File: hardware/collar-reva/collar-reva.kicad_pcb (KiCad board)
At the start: 2 copper layers, 30 x 30 mm, 0 parts

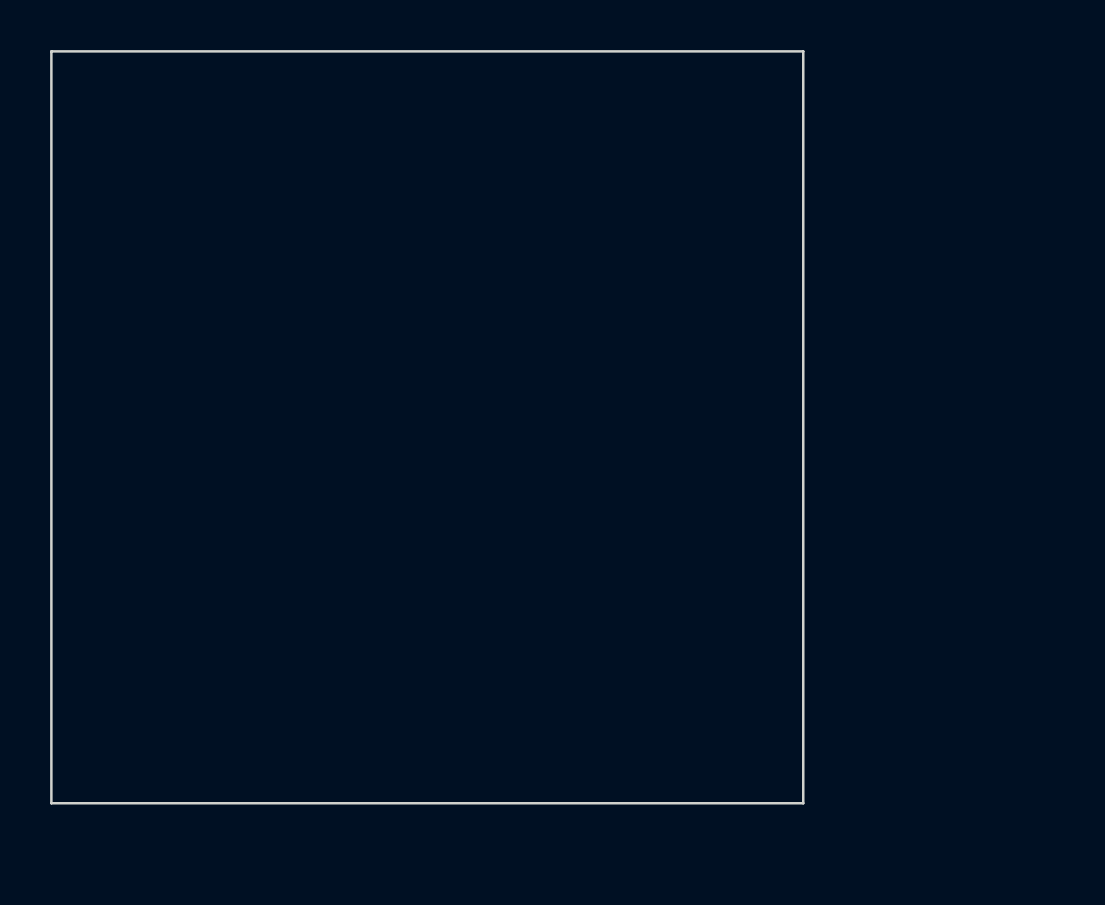
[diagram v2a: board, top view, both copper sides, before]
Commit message: feat(hw): place Rev-A parts on a 40×32 mm board
30×30 cannot fit the module and USB-C. Dirty/charge, brain, and optical zones are now footprints on the outline; copper is still unrouted.

Co-authored-by: Cursor <cursoragent@cursor.com>
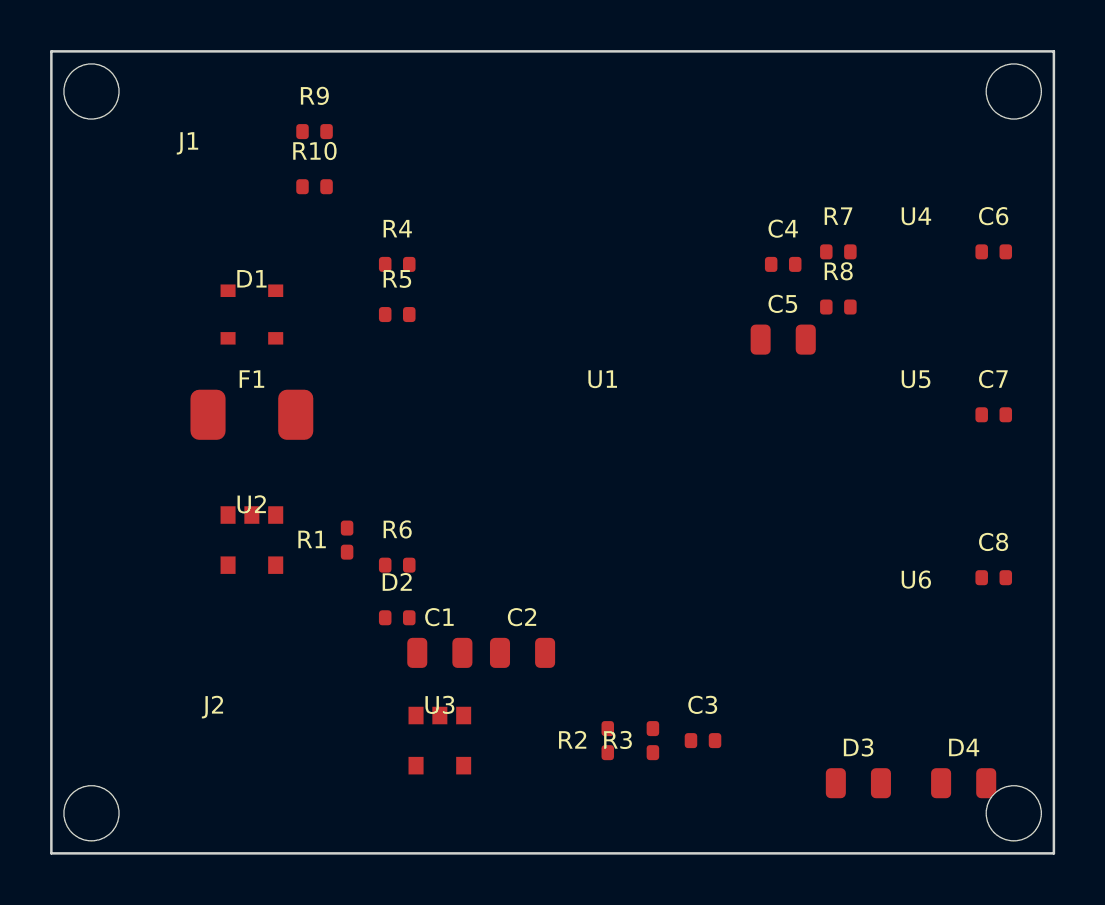
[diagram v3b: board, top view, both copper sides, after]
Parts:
- added C1: 10uF 16V, Capacitor_SMD:C_0805_2012Metric, F.Cu at (115.5, 104.0)
- added C2: 10uF 16V, Capacitor_SMD:C_0805_2012Metric, F.Cu at (118.8, 104.0)
- added C3: 100nF 16V, Capacitor_SMD:C_0402_1005Metric, F.Cu at (126.0, 107.5)
- added C4: 100nF 16V, Capacitor_SMD:C_0402_1005Metric, F.Cu at (129.2, 88.5)
- added C5: 10uF 16V, Capacitor_SMD:C_0805_2012Metric, F.Cu at (129.2, 91.5)
- added C6: 100nF 16V, Capacitor_SMD:C_0402_1005Metric, F.Cu at (137.6, 88.0)
- added C7: 100nF 16V, Capacitor_SMD:C_0402_1005Metric, F.Cu at (137.6, 94.5)
- added C8: 100nF 16V, Capacitor_SMD:C_0402_1005Metric, F.Cu at (137.6, 101.0)
- added D1: USBLC6-2SC6, Package_TO_SOT_SMD:SOT-23-6, F.Cu at (108.0, 90.5)
- added D2: Green LED, LED_SMD:LED_0402_1005Metric, F.Cu at (113.8, 102.6)
- added D3: 940 nm IR LED, LED_SMD:LED_0805_2012Metric, F.Cu at (132.2, 109.2)
- added D4: 940 nm photodiode, Diode_SMD:D_0805_2012Metric, F.Cu at (136.4, 109.2)
- added F1: PTC 500 mA, Fuse:Fuse_1812_4532Metric, F.Cu at (108.0, 94.5)
- added H: , MountingHole:MountingHole_2.2mm, F.Cu at (101.6, 81.6)
- added H: , MountingHole:MountingHole_2.2mm, F.Cu at (138.4, 81.6)
- added H: , MountingHole:MountingHole_2.2mm, F.Cu at (101.6, 110.4)
- added H: , MountingHole:MountingHole_2.2mm, F.Cu at (138.4, 110.4)
- added J1: USB-C receptacle, Connector_USB:USB_C_Receptacle_USB4105-xx-A_16P_TopMnt_Horizontal, F.Cu at (105.5, 85.0)
- added J2: JST-PH 2, Connector_JST:JST_PH_S2B-PH-SM4-TB_1x02-1MP_P2.00mm_Horizontal, F.Cu at (106.5, 107.5)
- added R1: 10k, Resistor_SMD:R_0402_1005Metric, F.Cu at (111.8, 99.5)
- added R10: 5.1k, Resistor_SMD:R_0402_1005Metric, F.Cu at (110.5, 85.4)
- added R2: 100k, Resistor_SMD:R_0402_1005Metric, F.Cu at (122.2, 107.5)
- added R3: 100k, Resistor_SMD:R_0402_1005Metric, F.Cu at (124.0, 107.5)
- added R4: 10k, Resistor_SMD:R_0402_1005Metric, F.Cu at (113.8, 88.5)
- added R5: 10k, Resistor_SMD:R_0402_1005Metric, F.Cu at (113.8, 90.5)
- added R6: 330, Resistor_SMD:R_0402_1005Metric, F.Cu at (113.8, 100.5)
- added R7: 4.7k, Resistor_SMD:R_0402_1005Metric, F.Cu at (131.4, 88.0)
- added R8: 4.7k, Resistor_SMD:R_0402_1005Metric, F.Cu at (131.4, 90.2)
- added R9: 5.1k, Resistor_SMD:R_0402_1005Metric, F.Cu at (110.5, 83.2)
- added U1: ESP32-S3-MINI-1-N8, RF_Module:ESP32-S3-MINI-1, F.Cu at (122.0, 94.5)
- added U2: MCP73831 4.2 V, Package_TO_SOT_SMD:SOT-23-5, F.Cu at (108.0, 99.5)
- added U3: AP2112K-3.3 600 mA, Package_TO_SOT_SMD:SOT-23-5, F.Cu at (115.5, 107.5)
- added U4: BMI270, Sensor_Motion:Bosch_LGA-14_2.5x3mm_P0.5mm_ClockwisePinNumbering, F.Cu at (134.5, 88.0)
- added U5: INMP441, Sensor_Audio:InvenSense_INMP441, F.Cu at (134.5, 94.5)
- added U6: AFE4404, Package_BGA:Texas_DSBGA-15_1.91x1.91mm_Layout5x3_P0.4mm, F.Cu at (134.5, 102.5)
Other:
- board size 30 x 30 mm -> 40 x 32 mm
- board text added: "RF_KEEP"

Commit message: feat(collar): emit gyro, die temp, and neck NTC on the 1 Hz map
The BMI270 and AFE already had unused channels. Turn them on and stuff the missing red LED plus contact NTC so the same notify map can carry chemistry-adjacent proxies without a new protocol.

Co-authored-by: Cursor <cursoragent@cursor.com>
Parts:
- added D5: 660 nm red LED, LED_SMD:LED_0805_2012Metric, F.Cu at (134.3, 106.8)
- added R11: 10k, Resistor_SMD:R_0402_1005Metric, F.Cu at (127.8, 106.8)
- added RT1: 10k NTC β3950, Resistor_SMD:R_0402_1005Metric, F.Cu at (127.8, 109.2)
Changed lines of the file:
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@@
+    )
+  )
+  (footprint "LED_SMD:LED_0805_2012Metric" (layer "F.Cu")
+    (at 134.3 106.8 0)
+    (attr smd)
+    (property "Reference" "D5" (at 0 -1.4 0)
+      (layer "F.SilkS")
+      (effects (font (size 0.7 0.7)))
+    )
+    (property "Value" "660 nm red LED" (at 0 1.4 0)
+      (layer "F.Fab")
+      (effects (font (size 0.6 0.6)))
+    )
+    (property "Footprint" "LED_SMD:LED_0805_2012Metric" (at 0 0 0)
+      (layer "F.Fab")
+      (effects (font (size 1.27 1.27)) hide)
+    )
+    (fp_rect (start -1.1 -0.8) (end 1.1 0.8)
+      (stroke (width 0.05) (type default)) (fill none) (layer "F.CrtYd")
+    )
+    (fp_rect (start -1.1 -0.8) (end 1.1 0.8)
+      (stroke (width 0.12) (type default)) (fill none) (layer "F.Fab")
+    )
+    (pad "1" smd roundrect (at -0.9 0) (size 0.8 1.2) (layers "F.Cu" "F.Paste" "F.Mask")
+      (roundrect_rratio 0.25)
+    )
+    (pad "2" smd roundrect (at 0.9 0) (size 0.8 1.2) (layers "F.Cu" "F.Paste" "F.Mask")
+      (roundrect_rratio 0.25)
+    )
+  )
+  (footprint "Resistor_SMD:R_0402_1005Metric" (layer "F.Cu")
+    (at 127.8 109.2 0)
+    (attr smd)
+    (property "Reference" "RT1" (at 0 -1.4 0)
+      (layer "F.SilkS")
+      (effects (font (size 0.7 0.7)))
+    )
+    (property "Value" "10k NTC β3950" (at 0 1.4 0)
+      (layer "F.Fab")
+      (effects (font (size 0.6 0.6)))
+    )
+    (property "Footprint" "Resistor_SMD:R_0402_1005Metric" (at 0 0 0)
+      (layer "F.Fab")
+      (effects (font (size 1.27 1.27)) hide)
+    )
+    (fp_rect (start -0.6 -0.45) (end 0.6 0.45)
+      (stroke (width 0.05) (type default)) (fill none) (layer "F.CrtYd")
+    )
+    (fp_rect (start -0.6 -0.45) (end 0.6 0.45)
+      (stroke (width 0.12) (type default)) (fill none) (layer "F.Fab")
+    )
+    (pad "1" smd roundrect (at -0.48 0) (size 0.5 0.6) (layers "F.Cu" "F.Paste" "F.Mask")
+      (roundrect_rratio 0.25)
+    )
+    (pad "2" smd roundrect (at 0.48 0) (size 0.5 0.6) (layers "F.Cu" "F.Paste" "F.Mask")
+      (roundrect_rratio 0.25)
+    )
+  )
+  (footprint "Resistor_SMD:R_0402_1005Metric" (layer "F.Cu")
+    (at 127.8 106.8 0)
+    (attr smd)
+    (property "Reference" "R11" (at 0 -1.4 0)
+      (layer "F.SilkS")
+      (effects (font (size 0.7 0.7)))
+    )
+    (property "Value" "10k" (at 0 1.4 0)
+      (layer "F.Fab")
+      (effects (font (size 0.6 0.6)))
+    )
+    (property "Footprint" "Resistor_SMD:R_0402_1005Metric" (at 0 0 0)
+      (layer "F.Fab")
+      (effects (font (size 1.27 1.27)) hide)
+    )
+    (fp_rect (start -0.6 -0.45) (end 0.6 0.45)
+      (stroke (width 0.05) (type default)) (fill none) (layer "F.CrtYd")
+    )
+    (fp_rect (start -0.6 -0.45) (end 0.6 0.45)
+      (stroke (width 0.12) (type default)) (fill none) (layer "F.Fab")
+    )
+    (pad "1" smd roundrect (at -0.48 0) (size 0.5 0.6) (layers "F.Cu" "F.Paste" "F.Mask")
+      (roundrect_rratio 0.25)
+    )
+    (pad "2" smd roundrect (at 0.48 0) (size 0.5 0.6) (layers "F.Cu" "F.Paste" "F.Mask")
+      (roundrect_rratio 0.25)
     )
   )

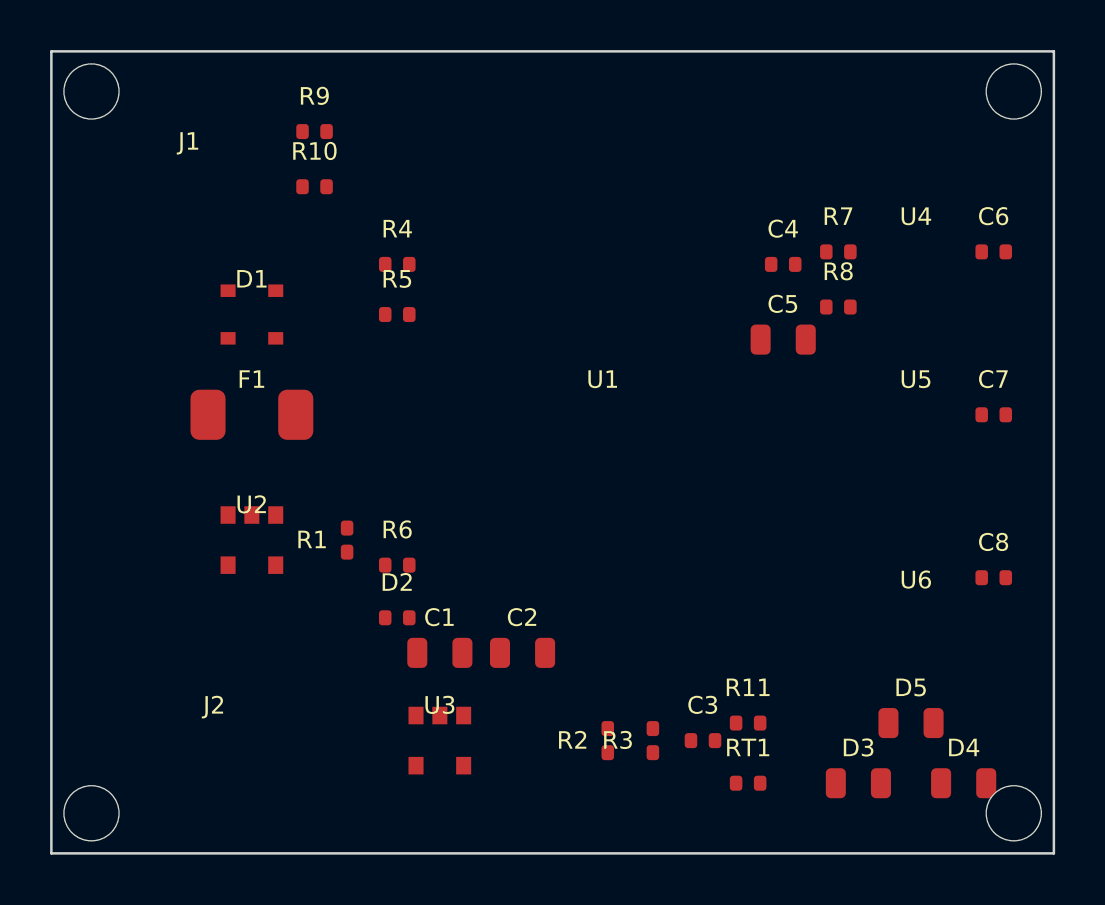
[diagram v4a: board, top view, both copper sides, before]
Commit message: feat(collar): read the red LED path and pour GND on Rev-A
D5 and LED2VAL were already programmed and stuffed. Emit red-channel perfusion on the existing notify map, and put F/B GND pours plus stitching vias on the 40×32 mm board. Not SpO2, and signals are still unrouted.

Co-authored-by: Cursor <cursoragent@cursor.com>
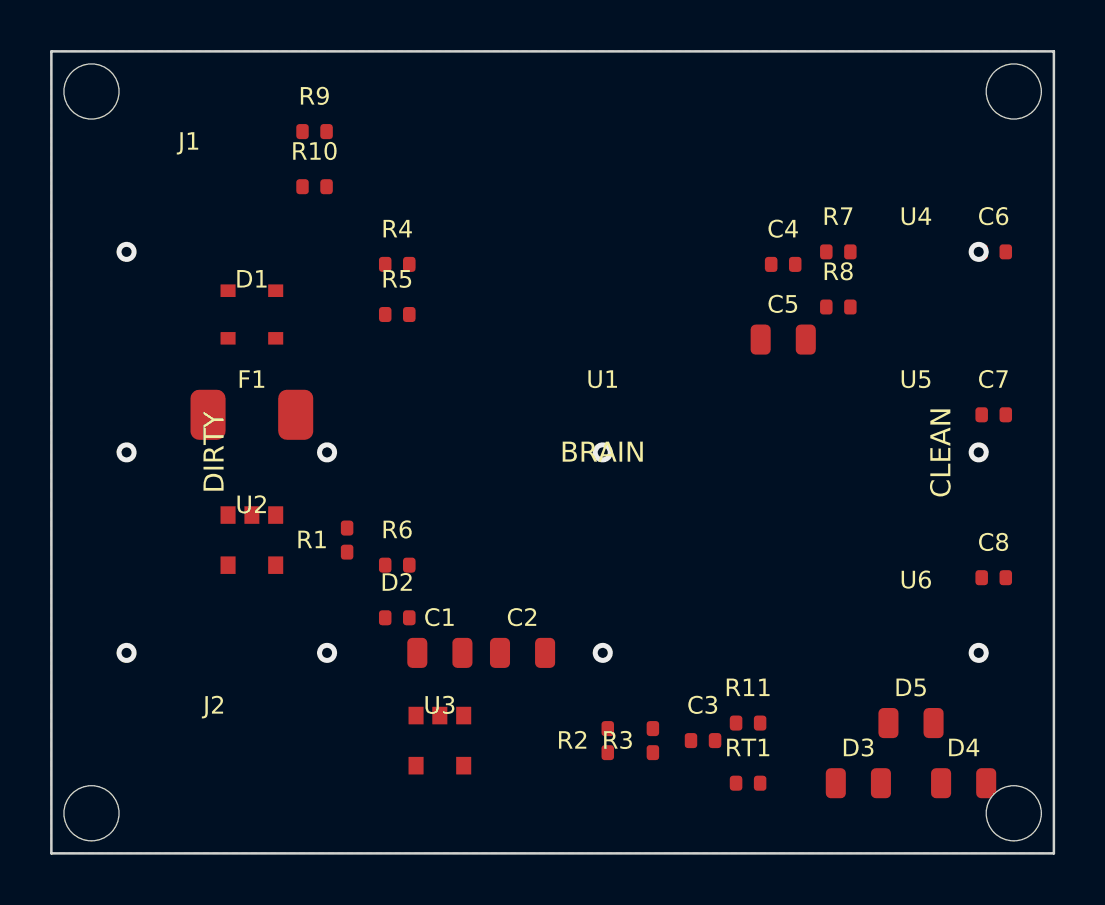
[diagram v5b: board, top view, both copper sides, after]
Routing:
- net GND: vias 0 -> 10
- added copper zone on B.Cu, net GND
- added copper zone on F.Cu, net GND
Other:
- board text added: "BRAIN"
- board text added: "CLEAN"
- board text added: "DIRTY"
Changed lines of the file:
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@@
     (pad_to_mask_clearance 0)
   )
+  (net 0 "")
+  (net 1 "GND")
+  (net 2 "3V3")
   (gr_rect (start 100.0 80.0) (end 140.0 112.0)
     (stroke (width 0.1) (type default)) (fill none) (layer "Edge.Cuts")
@@
   (gr_rect (start 114.0 80.4) (end 130.0 84.2)
     (stroke (width 0.1) (type default)) (fill none) (layer "Dwgs.User")
+  )
+  (gr_text "DIRTY" (at 106.5 96.0 90)
+    (layer "F.SilkS") (effects (font (size 0.8 0.8)))
+  )
+  (gr_text "BRAIN" (at 122.0 96.0 0)
+    (layer "F.SilkS") (effects (font (size 0.8 0.8)))
+  )
+  (gr_text "CLEAN" (at 135.5 96.0 90)
+    (layer "F.SilkS") (effects (font (size 0.8 0.8)))
   )
   (footprint "MountingHole:MountingHole_2.2mm" (layer "F.Cu")
@@
     )
   )
+  (via (at 103.0 88.0) (size 0.8) (drill 0.4) (layers "F.Cu" "B.Cu") (net 1)
+  )
+  (via (at 103.0 96.0) (size 0.8) (drill 0.4) (layers "F.Cu" "B.Cu") (net 1)
+  )
+  (via (at 103.0 104.0) (size 0.8) (drill 0.4) (layers "F.Cu" "B.Cu") (net 1)
+  )
+  (via (at 111.0 96.0) (size 0.8) (drill 0.4) (layers "F.Cu" "B.Cu") (net 1)
+  )
+  (via (at 111.0 104.0) (size 0.8) (drill 0.4) (layers "F.Cu" "B.Cu") (net 1)
+  )
+  (via (at 122.0 96.0) (size 0.8) (drill 0.4) (layers "F.Cu" "B.Cu") (net 1)
+  )
+  (via (at 122.0 104.0) (size 0.8) (drill 0.4) (layers "F.Cu" "B.Cu") (net 1)
+  )
+  (via (at 137.0 88.0) (size 0.8) (drill 0.4) (layers "F.Cu" "B.Cu") (net 1)
+  )
+  (via (at 137.0 96.0) (size 0.8) (drill 0.4) (layers "F.Cu" "B.Cu") (net 1)
+  )
+  (via (at 137.0 104.0) (size 0.8) (drill 0.4) (layers "F.Cu" "B.Cu") (net 1)
+  )
+  (zone (net 1) (net_name "GND") (layer "F.Cu") (hatch edge 0.508)
+    (connect_pads (clearance 0.2))
+    (min_thickness 0.25)
+    (filled_areas_thickness no)
+    (fill yes (thermal_gap 0.5) (thermal_bridge_width 0.5))
+    (polygon
+      (pts
+        (xy 100.0 80.0)
+        (xy 140.0 80.0)
+        (xy 140.0 112.0)
+        (xy 100.0 112.0)
+      )
+    )
+  )
+  (zone (net 1) (net_name "GND") (layer "B.Cu") (hatch edge 0.508)
+    (connect_pads (clearance 0.2))
+    (min_thickness 0.25)
+    (filled_areas_thickness no)
+    (fill yes (thermal_gap 0.5) (thermal_bridge_width 0.5))
+    (polygon
+      (pts
+        (xy 100.0 80.0)
+        (xy 140.0 80.0)
+        (xy 140.0 112.0)
+        (xy 100.0 112.0)
+      )
+    )
+  )
